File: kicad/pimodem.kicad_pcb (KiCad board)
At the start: 4 copper layers, 65 x 56.5 mm, 40 parts, among them J1 PWR_HEADER, J2 PI_HEADER, J3 SERIAL, J4 AUDIO_HEADER, J5 LED_PANEL, J6 WP, J7 GAIN, Q1 DMG2305UX, Q2 BC857BS, Q3 DMG3414U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

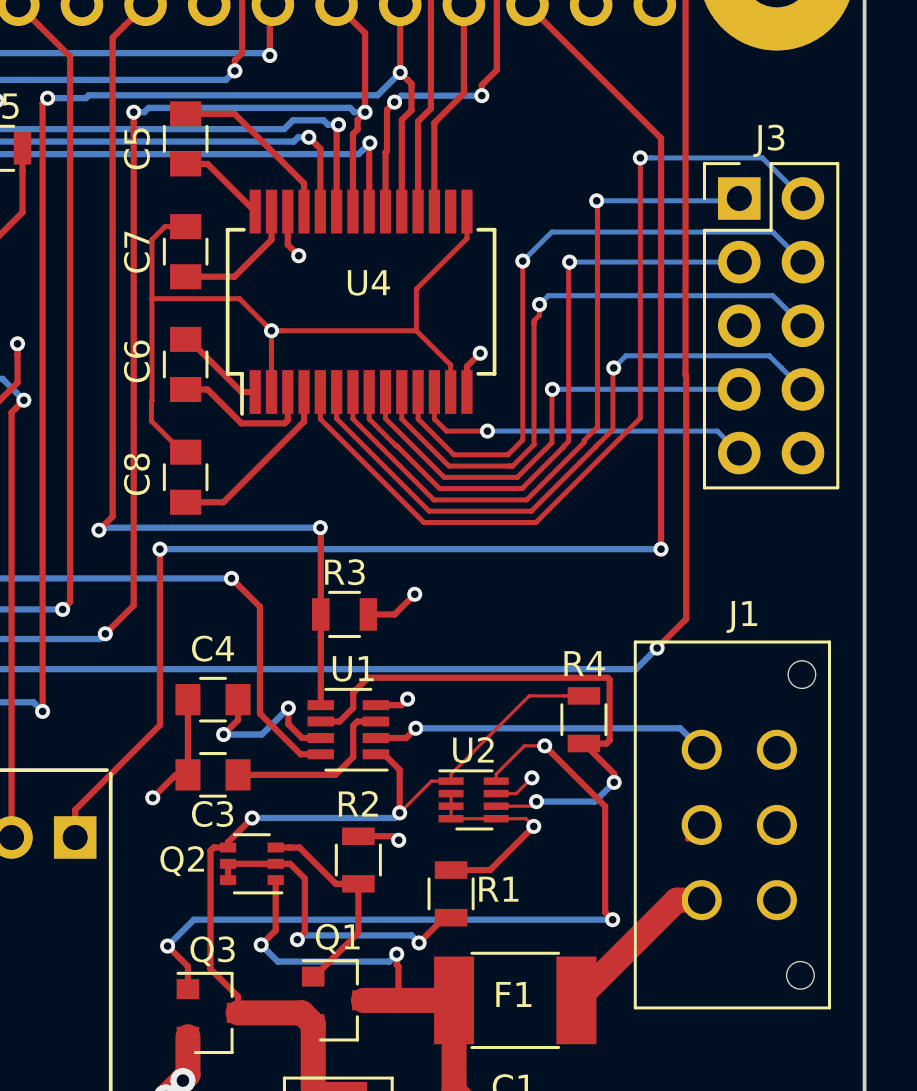
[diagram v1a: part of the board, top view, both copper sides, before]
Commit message: Update traces for serial header to use DTK/intel format
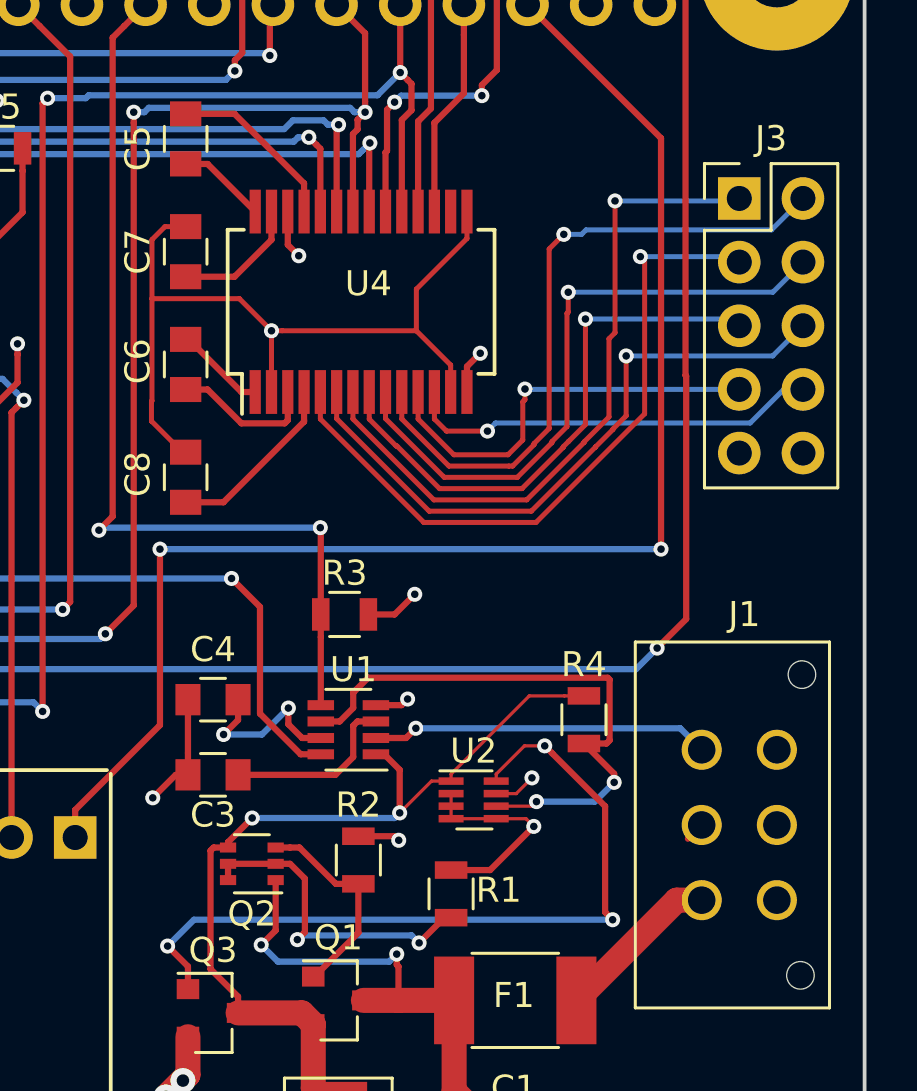
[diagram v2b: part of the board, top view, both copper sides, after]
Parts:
- Q2: footprint TO_SOT_Packages_SMD:SOT-363_SC-70-6 -> Package_TO_SOT_SMD:SOT-363_SC-70-6
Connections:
- J3 pad 5: GND -> Net-(J3-Pad5)
- J3 pad 9: Net-(J3-Pad9) -> GND
- U4 pad 10: Net-(J3-Pad6) -> Net-(J3-Pad2)
- U4 pad 11: Net-(J3-Pad4) -> Net-(J3-Pad7)
- U4 pad 12: Net-(J3-Pad9) -> Net-(J3-Pad8)
- U4 pad 5: Net-(J3-Pad2) -> Net-(J3-Pad3)
- U4 pad 6: Net-(J3-Pad8) -> Net-(J3-Pad6)
- U4 pad 8: Net-(J3-Pad3) -> Net-(J3-Pad5)
- U4 pad 9: Net-(J3-Pad7) -> Net-(J3-Pad4)
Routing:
- net Net-(J3-Pad5): track 0.00 -> 22.4 mm, vias 0 -> 1
- net Net-(J3-Pad9): track 14.0 -> 0.00 mm, vias 1 -> 0
- net Net-(J3-Pad8): track 25.7 -> 16.7 mm
- net Net-(J3-Pad2): track 34.8 -> 26.5 mm
- net Net-(J3-Pad3): track 24.9 -> 27.8 mm
- net Net-(J3-Pad7): track 18.8 -> 16.7 mm
- net Net-(J3-Pad6): track 24.3 -> 25.7 mm

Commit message: kicad: Update schematic and pcb layout
* Connect serial gpio signals through inverter gates
* Connect all leds to gpio pins
* Update eeprom to 24c512
* Update pcb footprints to new names (kicad update)
* Update schematic/board revision to 1.2
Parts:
- removed J6: WP, Pin_Headers:Pin_Header_Straight_1x02_Pitch2.54mm
- added R10: 0Ohm, Resistor_SMD:R_0805_2012Metric, F.Cu at (45.5, 37.1)
- C1, C2, C3, C4, C5, C6, C7, C8, C9: footprint Capacitors_SMD:C_0805 -> Capacitor_SMD:C_0805_2012Metric
- D1: footprint Diodes_SMD:D_SMB_Standard -> Diode_SMD:D_SMB
- F1: footprint Resistors_SMD:R_1812 -> Resistor_SMD:R_1812_4532Metric
- J1: footprint Connectors_Molex:Molex_Microfit3_Header_02x03_Straight_43045-0628 -> Connector_Molex:Molex_Micro-Fit_3.0_43045-0612_2x03_P3.00mm_Vertical
- J2: footprint Socket_Strips:Socket_Strip_Straight_2x20_Pitch2.54mm -> Connector_PinSocket_2.54mm:PinSocket_2x20_P2.54mm_Vertical
- J3, J5: footprint Pin_Headers:Pin_Header_Straight_2x05_Pitch2.54mm -> Connector_PinHeader_2.54mm:PinHeader_2x05_P2.54mm_Vertical
- J7: footprint Pin_Headers:Pin_Header_Straight_2x04_Pitch2.54mm -> Connector_PinHeader_2.54mm:PinHeader_2x04_P2.54mm_Vertical
- Q1, Q3: footprint TO_SOT_Packages_SMD:SOT-23 -> Package_TO_SOT_SMD:SOT-23
- R1, R2, R3, R4, R5, R6, R7, R8, R9: footprint Resistors_SMD:R_0805 -> Resistor_SMD:R_0805_2012Metric
- U1: footprint TO_SOT_Packages_SMD:SOT-23-8 -> Package_TO_SOT_SMD:SOT-23-8
- U2: footprint TO_SOT_Packages_SMD:SC-70-8 -> Package_TO_SOT_SMD:SC-70-8
- U3: footprint Housings_SOIC:SOIC-18W_7.5x11.6mm_Pitch1.27mm -> Package_SO:SOIC-18W_7.5x11.6mm_P1.27mm
- U4: footprint Housings_SSOP:SSOP-28_5.3x10.2mm_Pitch0.65mm -> Package_SO:SSOP-28_5.3x10.2mm_P0.65mm
- U5: footprint Housings_SOIC:SOIC-14_3.9x8.7mm_Pitch1.27mm -> Package_SO:SOIC-14_3.9x8.7mm_P1.27mm
- U6: value 24LC32 -> 24LC512; footprint Housings_SOIC:SOIC-8_3.9x4.9mm_Pitch1.27mm -> Package_SO:SOIC-8_3.9x4.9mm_P1.27mm
- turned J1 to 90 degrees
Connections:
- net LED2 renamed ACT
- net LED7 renamed SD
- net LED8 renamed RD
- J2 pad 13: Net-(J2-Pad13) -> AA
- J2 pad 15: Net-(J2-Pad15) -> OH
- J2 pad 29: DCD -> CD
- U3 pad 1: DSR -> CD
- U3 pad 3: DCD -> DTR
- U3 pad 4: LED4 -> DSR
- U3 pad 5: LED5 -> OH
- U3 pad 6: LED6 -> AA
- U4 pad 17: RI -> Net-(U4-Pad17)
- U4 pad 18: DTR -> Net-(U4-Pad18)
- U4 pad 19: DSR -> Net-(U4-Pad19)
- U4 pad 22: DCD -> Net-(U4-Pad22)
- U5 pad 10: Net-(U5-Pad10) -> Net-(U4-Pad19)
- U5 pad 11: GND -> DSR
- U5 pad 12: Net-(U5-Pad12) -> DTR
- U5 pad 13: GND -> Net-(U4-Pad18)
- U5 pad 5: GND -> CD
- U5 pad 6: Net-(U5-Pad6) -> Net-(U4-Pad22)
- U5 pad 8: Net-(U5-Pad8) -> Net-(U4-Pad17)
- U5 pad 9: GND -> RI
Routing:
- net CD: track 0.00 -> 71.4 mm, vias 0 -> 2
- net DTR: track 11.5 -> 76.1 mm, vias 0 -> 4
- net DCD: track 55.5 -> 0.00 mm, vias 4 -> 0
- net Net-(U4-Pad18): track 0.00 -> 47.1 mm, vias 0 -> 2
- net Net-(U4-Pad19): track 0.00 -> 40.8 mm, vias 0 -> 2
- net Net-(U4-Pad17): track 0.00 -> 39.4 mm, vias 0 -> 2
- net OH: track 0.00 -> 39.1 mm, vias 0 -> 1
- net Net-(U4-Pad22): track 0.00 -> 38.2 mm, vias 0 -> 2
- net RI: track 8.74 -> 44.5 mm, vias 0 -> 2
- net AA: track 0.00 -> 33.3 mm, vias 0 -> 1
- net GND: track 103.0 -> 85.8 mm
- net DSR: track 60.8 -> 71.1 mm
- net +3V3: track 19.4 -> 22.5 mm, vias 8 -> 7
- net (no net): track 2.20 -> 0.00 mm
- net SD: track 60.5 -> 61.7 mm
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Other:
- net class Default: clearance 0.25 -> 0.16; via_dia 0.8 -> 0.6; via_drill 0.4 -> 0.3
- rule trace_clearance: 0.25 -> 0.16
- rule trace_min: 0.13 -> 0.16
- board text added: "PiModem"
- board text added: "Rev 1.3"
